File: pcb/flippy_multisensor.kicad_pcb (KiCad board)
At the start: 2 copper layers, 65.4 x 23.2 mm, 21 parts, among them J1 PINHD_1x8_Male, J2 PINHD_1x10_Male, U1 SHT30-DIS-B10KS, U2 LSM6DS3TR-C, U3 PA1010D

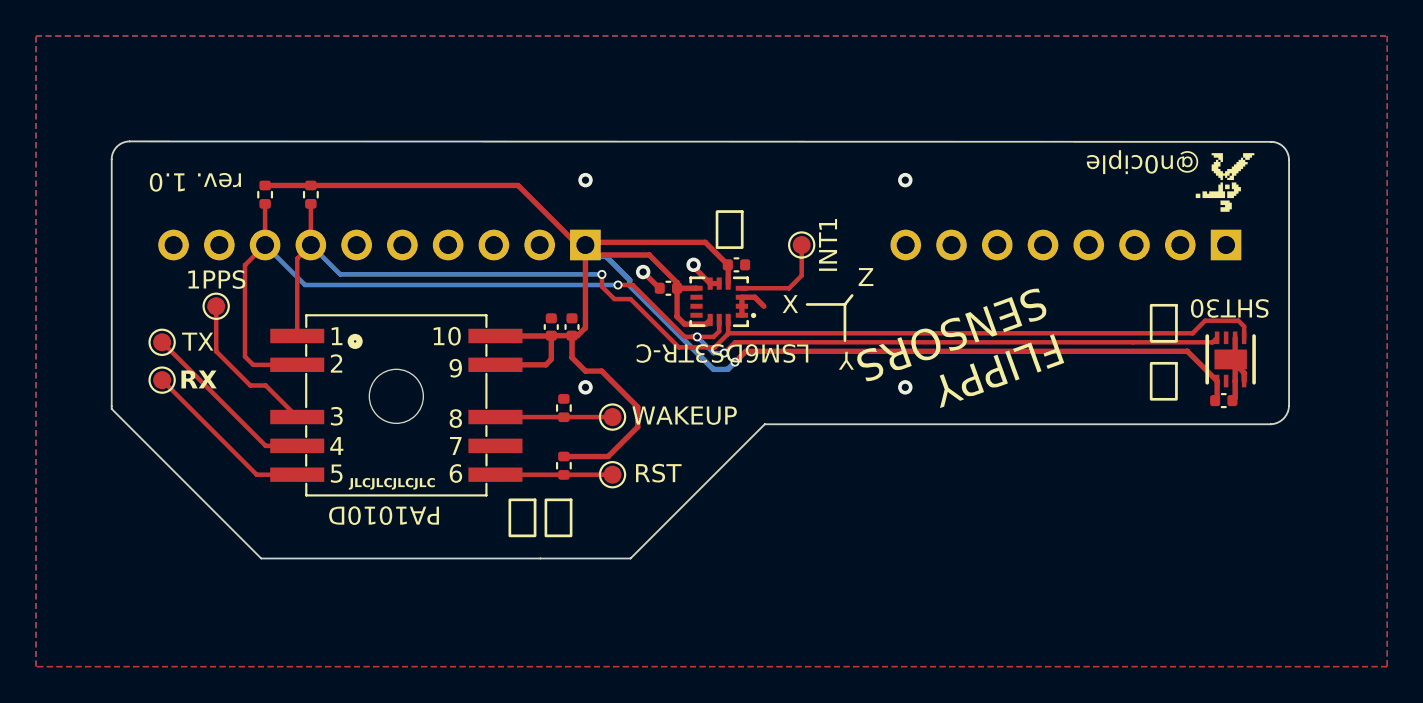
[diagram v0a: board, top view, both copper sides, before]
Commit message: update test points labels
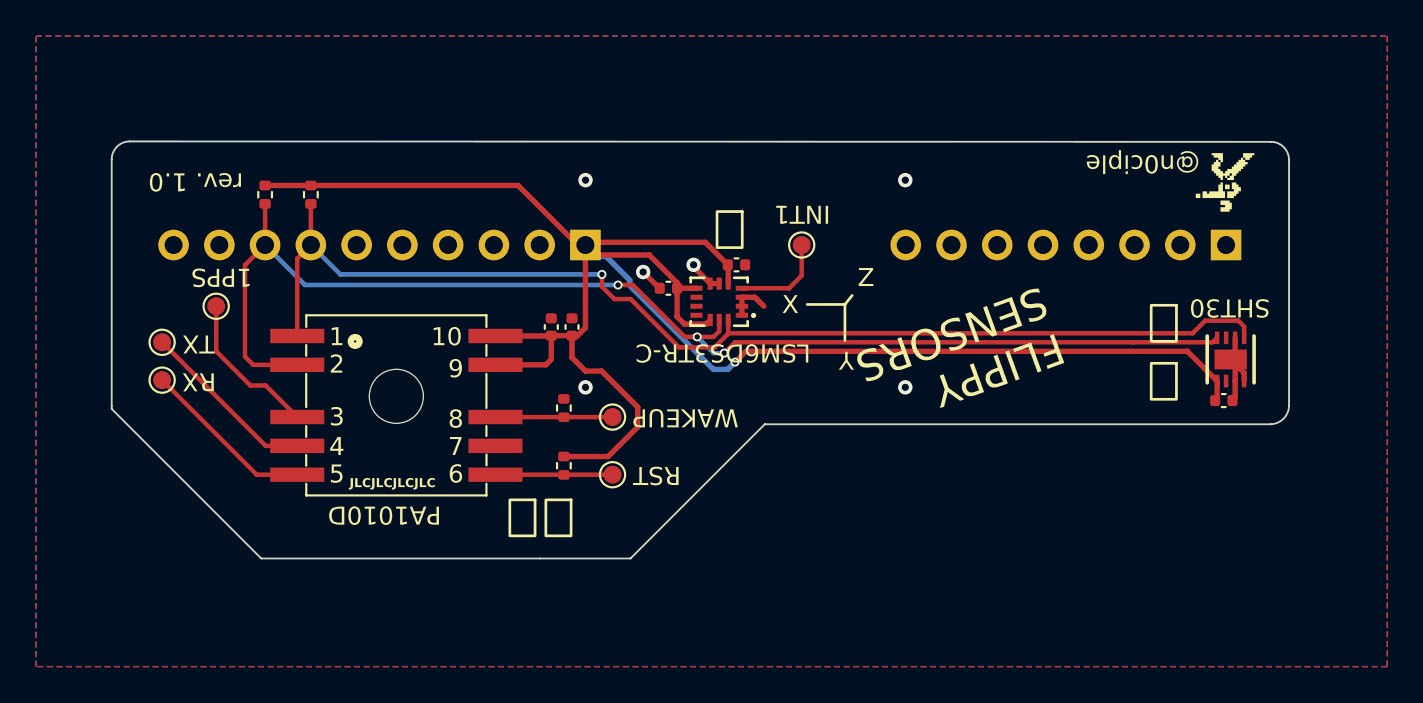
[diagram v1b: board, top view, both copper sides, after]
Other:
- board text added: "1PPS"
- board text added: "INT1"
- board text added: "RST"
- board text added: "RX"
- board text added: "TX"
- board text added: "WAKEUP"

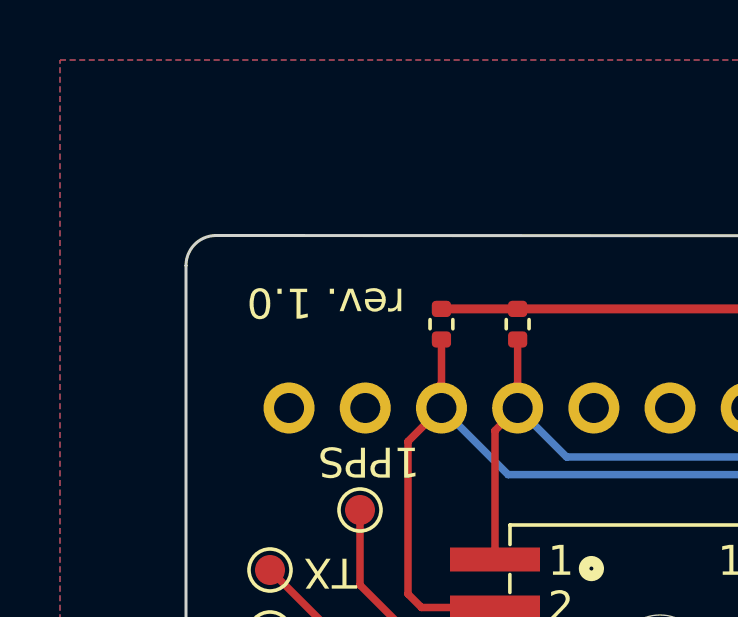
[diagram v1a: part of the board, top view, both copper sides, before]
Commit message: correct the SHT30 i2c address on the label
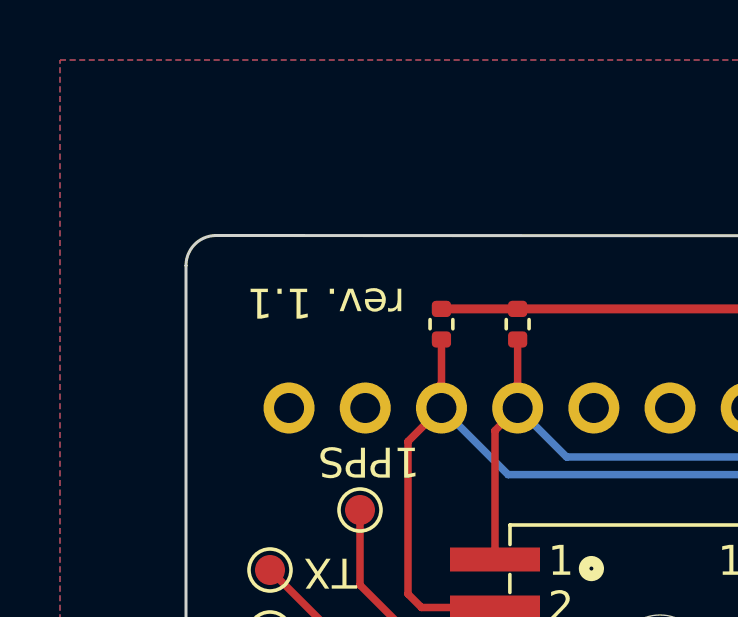
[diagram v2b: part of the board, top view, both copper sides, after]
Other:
- board text added: "I2C Addresses: SHT30 0x44 LSM6DS3TR-C 0x6A PA1010D 0x10"
- board text added: "rev. 1.1"
- board text removed: "I2C Addresses: SHT30 0x45 LSM6DS3TR-C 0x6A PA1010D 0x10"
- board text removed: "rev. 1.0"
